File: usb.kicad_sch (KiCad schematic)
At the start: 3 parts, among them J4 USB_C_Receptacle_PowerOnly_6P

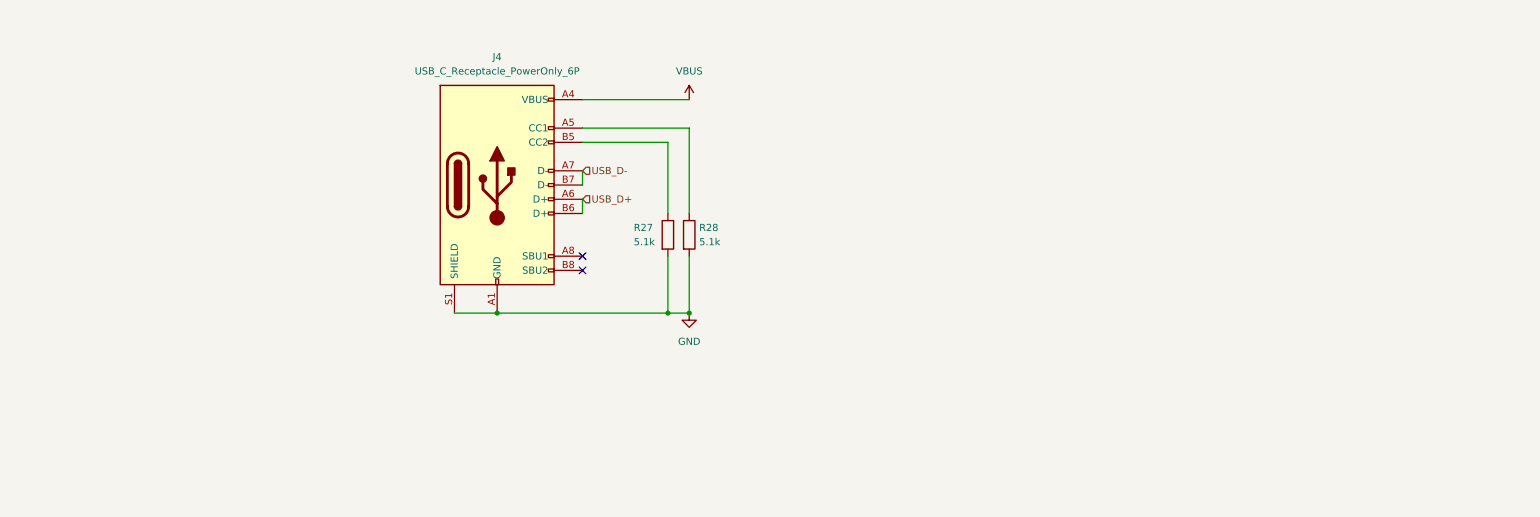
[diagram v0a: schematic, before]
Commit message: add audio amp
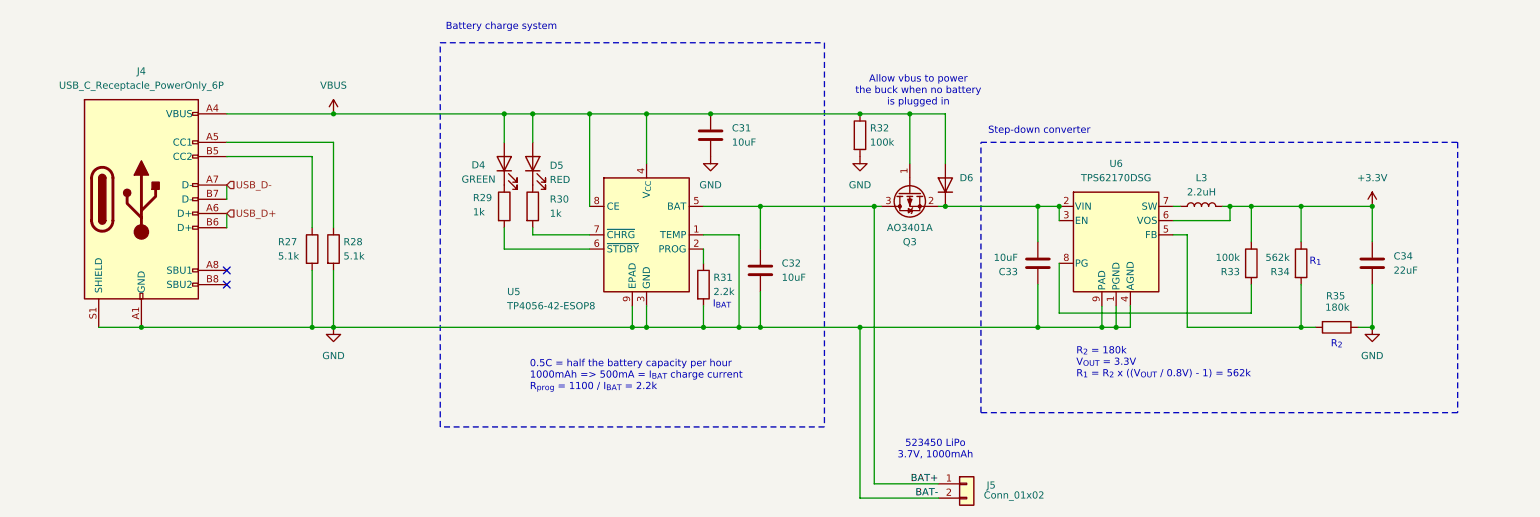
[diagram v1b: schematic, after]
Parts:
- added C31, C32, C33: 10uF, Capacitor_SMD:C_0603_1608Metric, symbol Device:C
- added C34: 22uF, Capacitor_SMD:C_0603_1608Metric, symbol Device:C
- added D4: GREEN, LED_SMD:LED_0603_1608Metric, symbol Device:LED
- added D5: RED, LED_SMD:LED_0603_1608Metric, symbol Device:LED
- added D6: D, Diode_SMD:D_SOD-323, symbol Device:D
- added J5: Conn_01x02, Connector_JST:JST_PH_B2B-PH-K_1x02_P2.00mm_Vertical, symbol Connector_Generic:Conn_01x02
- added L3: 2.2uH, Inductor_SMD:L_KOHERelec_MDA7030, symbol Device:L
- added Q3: AO3401A, Package_TO_SOT_SMD:SOT-23, symbol Transistor_FET:AO3401A
- added R29, R30: 1k, Resistor_SMD:R_0603_1608Metric, symbol Device:R
- added R31: 2.2k, Resistor_SMD:R_0603_1608Metric, symbol Device:R
- added R32, R33: 100k, Resistor_SMD:R_0603_1608Metric, symbol Device:R
- added R34: 562k, Resistor_SMD:R_0603_1608Metric, symbol Device:R
- added R35: 180k, Resistor_SMD:R_0603_1608Metric, symbol Device:R
- added U5: TP4056-42-ESOP8, Package_SO:SOIC-8-1EP_3.9x4.9mm_P1.27mm_EP2.41x3.3mm_ThermalVias, symbol Battery_Management:TP4056-42-ESOP8
- added U6: TPS62170DSG, Package_SON:WSON-8-1EP_2x2mm_P0.5mm_EP0.9x1.6mm_ThermalVias, symbol Regulator_Switching:TPS62170DSG
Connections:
- net GND: now also C31.2, C32.2, C33.2, C34.2, J5.2 (Pin_2), R31.2, R32.2, R35.1, U5.1 (TEMP), U5.3 (GND), U5.9 (EPAD), U6.1 (PGND), U6.4 (AGND), U6.9 (PAD)
- net VBUS: now also C31.1, D4.2 (A), D5.2 (A), D6.2 (A), Q3.1 (G), R32.1, U5.4 (V_{CC}), U5.8 (CE)
- new net: R33.2, U6.8 (PG)
- new net: D5.1 (K), R30.1
- new net: C33.1, D6.1 (K), Q3.2 (S), U6.2 (VIN), U6.3 (EN)
- new net: R31.1, U5.2 (PROG)
- new net: R29.2, U5.6 (~{STDBY})
- new net: R30.2, U5.7 (~{CHRG})
- new net: D4.1 (K), R29.1
- new net: R34.2, R35.2, U6.5 (FB)
- new net: L3.1, U6.7 (SW)
- new net +3.3V: C34.1, L3.2, R33.1, R34.1, U6.6 (VOS)
- new net BAT+: C32.1, J5.1 (Pin_1), Q3.3 (D), U5.5 (BAT)
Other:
- note added: "0.5C = half the battery capacity per hour 1000mAh => 500mA = I_{BAT} charge current R_{prog} = 1100 / I_{BAT} = 2.2k"
- note added: "523450 LiPo 3.7V, 1000mAh"
- note added: "Allow vbus to power the buck when no battery is plugged in"
- note added: "Battery charge system"
- note added: "I_{BAT}"
- note added: "R_{1}"
- note added: "R_{2}"
- note added: "R_{2} = 180k V_{OUT} = 3.3V R_{1} = R_{2} x ((V_{OUT} / 0.8V) - 1) = 562k"
- note added: "Step-down converter"
- moved on the sheet: J4, R27, R28

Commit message: add amplifier mode selector, add drawing lcd
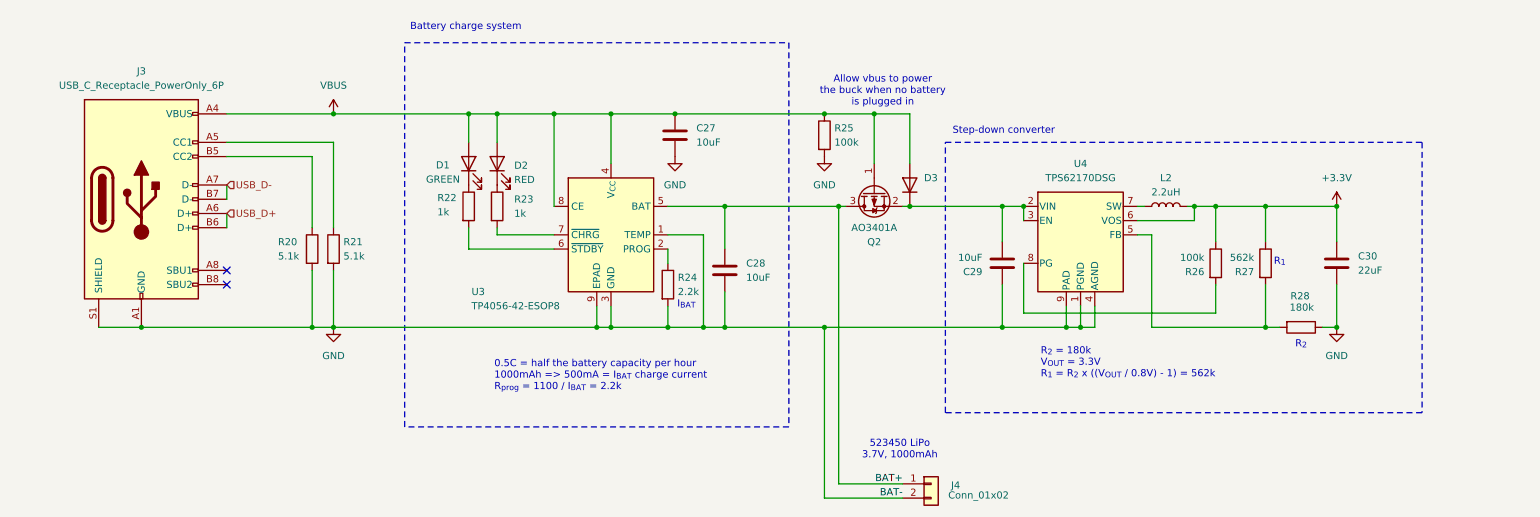
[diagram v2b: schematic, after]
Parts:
- renumbered C31 to C27, C32 to C28, C33 to C29, C34 to C30, D4 to D1, D5 to D2, D6 to D3, J4 to J3, J5 to J4, L3 to L2, Q3 to Q2, R27 to R20, R28 to R21, R29 to R22, R30 to R23, R31 to R24, R32 to R25, R33 to R26, R34 to R27, R35 to R28, U5 to U3, U6 to U4
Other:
- moved on the sheet: C27, C28, C29, C30, D1, D2, D3, J4, L2, Q2, R22, R23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

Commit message: add on/off switch
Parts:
- added SW12: SW_SPST, symbol Switch:SW_SPST
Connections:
- net +5V: now reaches C29.1, U4.2 (VIN), U4.3 (EN)
- net +5V: now also SW12.2 (B); no longer D3.1 (K), Q2.2 (S)
- new net: D3.1 (K), Q2.2 (S), SW12.1 (A)
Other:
- moved on the sheet: C27, C28, C29, C30, D1, D2, D3, J3, J4, L2, Q2, R20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

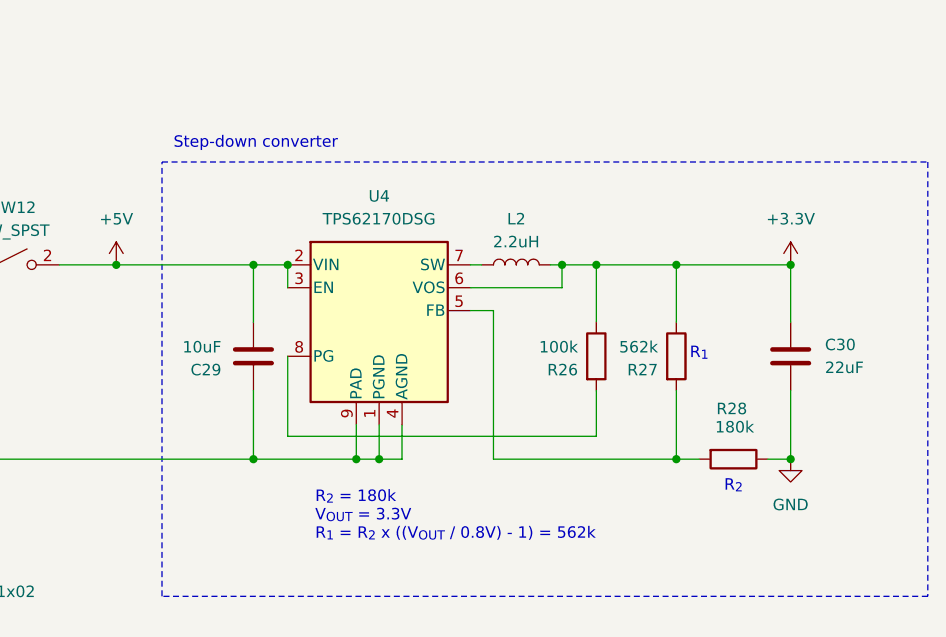
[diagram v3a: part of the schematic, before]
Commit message: add vibration motor
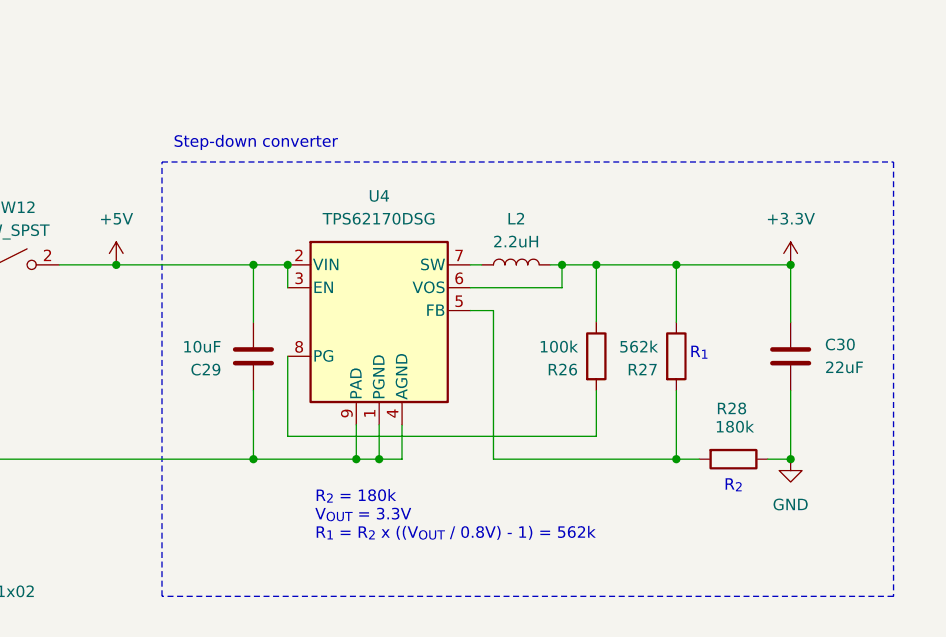
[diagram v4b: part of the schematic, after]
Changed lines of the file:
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@@
 	(rectangle
 		(start 198.12 73.66)
-		(end 283.21 121.92)
+		(end 279.4 121.92)
 		(stroke
 			(width 0)

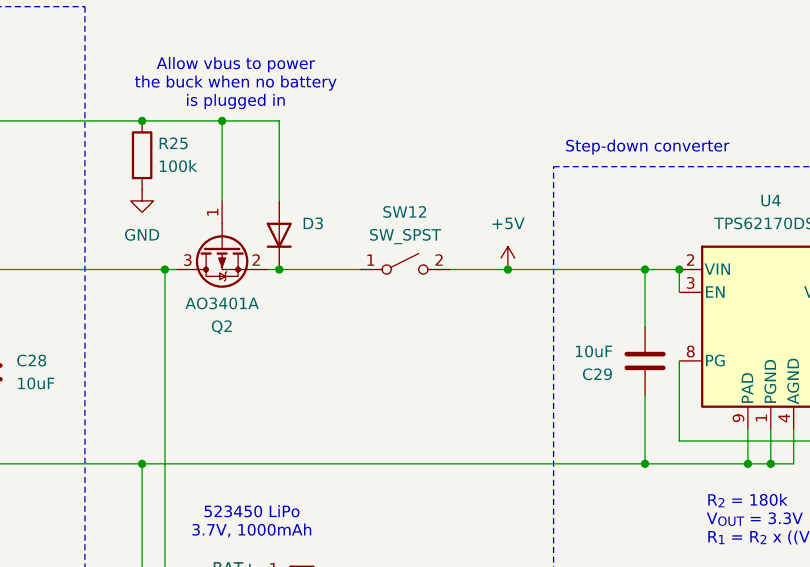
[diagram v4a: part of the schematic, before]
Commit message: add SD card
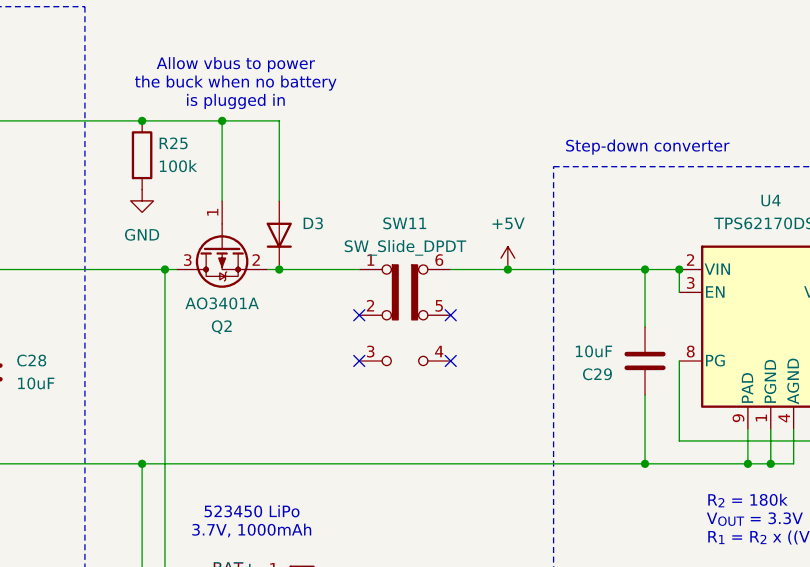
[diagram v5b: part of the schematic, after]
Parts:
- removed SW12: SW_SPST, symbol Switch:SW_SPST
- added SW11: SW_Slide_DPDT, Button_Switch_SMD:SW_DPDT_CK_JS202011JCQN, symbol Switch:SW_Slide_DPDT
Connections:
- net +5V: now also SW11.6 (C)
- net at D3.1 (K), Q2.2 (S): now also SW11.1 (A)
- no-connect marks 2 -> 6
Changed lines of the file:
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@@
+	)
+	(no_connect
+		(at 176.53 90.17)
+	)
+	(no_connect
+		(at 186.69 95.25)
+	)
+	(no_connect
+		(at 186.69 90.17)
 	)
 	(no_connect
 		(at 45.72 99.06)
+	)
+	(no_connect
+		(at 176.53 95.25)
 	)
 	(no_connect
@@
 	)
 	(symbol
-		(lib_id "Switch:SW_SPST")
-		(at 181.61 85.09 0)
+		(lib_id "Switch:SW_Slide_DPDT")
+		(at 181.61 90.17 0)
 		(unit 1)
 		(exclude_from_sim no)
@@
 		(dnp no)
 		(fields_autoplaced yes)
-		(property "Reference" "SW12"
-			(at 181.61 78.74 0)
-			(effects
-				(font
-					(size 1.27 1.27)
-				)
-			)
-		)
-		(property "Value" "SW_SPST"
-			(at 181.61 81.28 0)
-			(effects
-				(font
-					(size 1.27 1.27)
-				)
-			)
-		)
-		(property "Footprint" ""
-			(at 181.61 85.09 0)
+		(property "Reference" "SW11"
+			(at 181.61 80.01 0)
+			(effects
+				(font
+					(size 1.27 1.27)
+				)
+			)
+		)
+		(property "Value" "SW_Slide_DPDT"
+			(at 181.61 82.55 0)
+			(effects
+				(font
+					(size 1.27 1.27)
+				)
+			)
+		)
+		(property "Footprint" "Button_Switch_SMD:SW_DPDT_CK_JS202011JCQN"
+			(at 195.58 85.09 0)
 			(effects
 				(font
@@
 		)
 		(property "Datasheet" "~"
-			(at 181.61 85.09 0)
-			(effects
-				(font
-					(size 1.27 1.27)
-				)
-				(hide yes)
-			)
-		)
-		(property "Description" "Single Pole Single Throw (SPST) switch"
-			(at 181.61 85.09 0)
-			(effects
-				(font
-					(size 1.27 1.27)
-				)
-				(hide yes)
-			)
+			(at 181.61 90.17 0)
+			(effects
+				(font
+					(size 1.27 1.27)
+				)
+				(hide yes)
+			)
+		)
+		(property "Description" "Slide Switch, dual pole double throw"
+			(at 181.61 90.17 0)
+			(effects
+				(font
+					(size 1.27 1.27)
+				)
+				(hide yes)
+			)
+		)
+		(property "LCSC" "C221665"
+			(at 181.61 90.17 0)
+			(effects
+				(font
+					(size 1.27 1.27)
+				)
+				(hide yes)
+			)
+		)
+		(property "Manufacturer" "C&K"
+			(at 181.61 90.17 0)
+			(effects
+				(font
+					(size 1.27 1.27)
+				)
+				(hide yes)
+			)
+		)
+		(property "Manufacturer Part Number" "JS202011JCQN"
+			(at 181.61 90.17 0)
+			(effects
+				(font
+					(size 1.27 1.27)
+				)
+				(hide yes)
+			)
+		)
+		(pin "3"
+		)
+		(pin "6"
+		)
+		(pin "4"
+		)
+		(pin "1"
 		)
 		(pin "2"
 		)
-		(pin "1"
+		(pin "5"
 		)
 		(instances
 			(project ""
 				(path "/f4643692-c319-40a7-82a2-3e775c0a417f/14ac419d-87de-4e8e-be3d-9259b1e7c76f"
-					(reference "SW12")
+					(reference "SW11")
 					(unit 1)
 				)

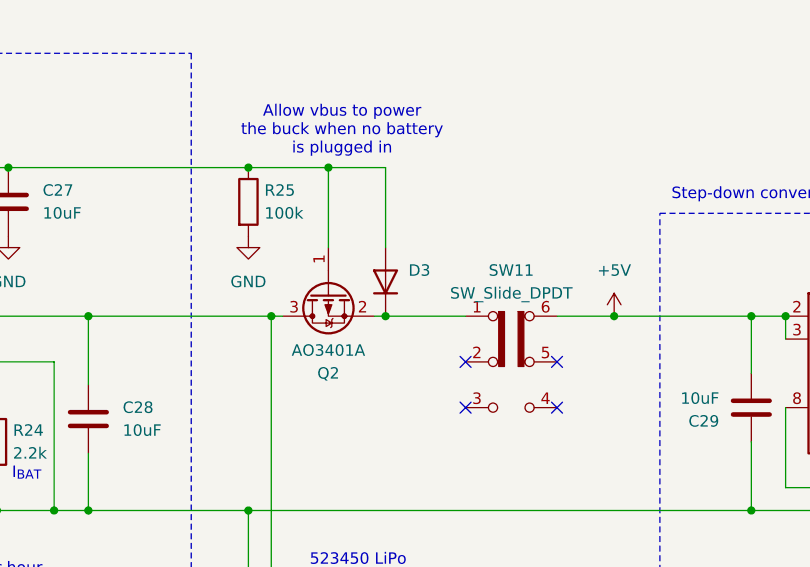
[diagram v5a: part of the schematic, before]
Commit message: small updates in component selection
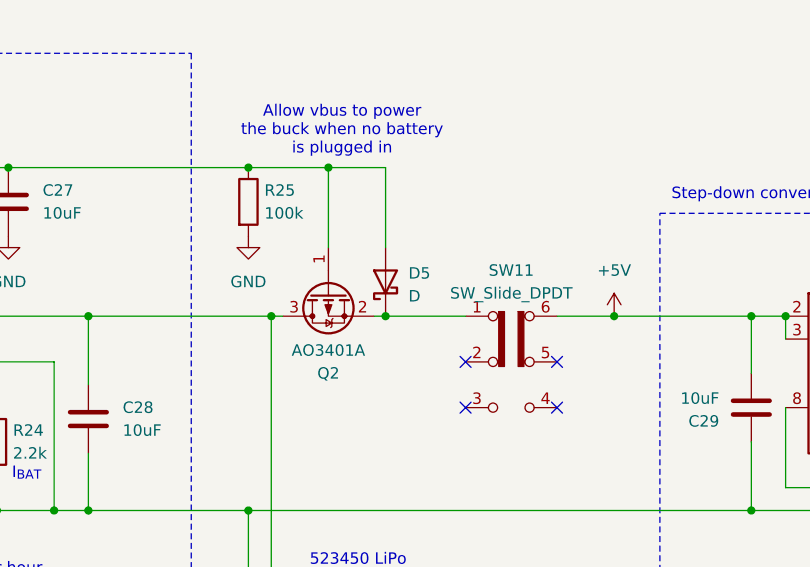
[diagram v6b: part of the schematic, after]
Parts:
- removed D3: D, Diode_SMD:D_SOD-323, symbol Device:D
- added D5: D, Diode_SMD:D_SMA, symbol Device:D_Schottky
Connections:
- net VBUS: now also D5.2 (A)
- net at Q2.2 (S), SW11.1 (A): now also D5.1 (K)
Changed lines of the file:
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@@
 	)
 	(junction
-		(at 114.3 106.68)
+		(at 167.64 85.09)
 		(diameter 0)
 		(color 0 0 0 0)
 	)
 	(junction
-		(at 167.64 85.09)
+		(at 114.3 106.68)
 		(diameter 0)
 		(color 0 0 0 0)
@@
 	(wire
 		(pts
+			(xy 167.64 85.09) (xy 176.53 85.09)
+		)
+		(stroke
+			(width 0)
+			(type default)
+		)
+	)
+	(wire
+		(pts
 			(xy 186.69 85.09) (xy 193.04 85.09)
 		)
@@
 	(wire
 		(pts
-			(xy 167.64 85.09) (xy 176.53 85.09)
-		)
-		(stroke
-			(width 0)
-			(type default)
-		)
-	)
-	(wire
-		(pts
 			(xy 111.76 102.87) (xy 111.76 106.68)
 		)
@@
 	)
 	(symbol
+		(lib_id "Device:D_Schottky")
+		(at 167.64 81.28 90)
+		(unit 1)
+		(exclude_from_sim no)
+		(in_bom yes)
+		(on_board yes)
+		(dnp no)
+		(fields_autoplaced yes)
+		(property "Reference" "D5"
+			(at 170.18 80.3274 90)
+			(effects
+				(font
+					(size 1.27 1.27)
+				)
+				(justify right)
+			)
+		)
+		(property "Value" "D"
+			(at 170.18 82.8674 90)
+			(effects
+				(font
+					(size 1.27 1.27)
+				)
+				(justify right)
+			)
+		)
+		(property "Footprint" "Diode_SMD:D_SMA"
+			(at 167.64 81.28 0)
+			(effects
+				(font
+					(size 1.27 1.27)
+				)
+				(hide yes)
+			)
+		)
+		(property "Datasheet" "~"
+			(at 167.64 81.28 0)
+			(effects
+				(font
+					(size 1.27 1.27)
+				)
+				(hide yes)
+			)
+		)
+		(property "Description" "Schottky diode"
+			(at 167.64 81.28 0)
+			(effects
+				(font
+					(size 1.27 1.27)
+				)
+				(hide yes)
+			)
+		)
+		(property "Sim.Device" "D"
+			(at 167.64 81.28 0)
+			(effects
+				(font
+					(size 1.27 1.27)
+				)
+				(hide yes)
+			)
+		)
+		(property "Sim.Pins" "1=K 2=A"
+			(at 167.64 81.28 0)
+			(effects
+				(font
+					(size 1.27 1.27)
+				)
+				(hide yes)
+			)
+		)
+		(property "LCSC" "C64982"
+			(at 167.64 81.28 0)
+			(effects
+				(font
+					(size 1.27 1.27)
+				)
+				(hide yes)
+			)
+		)
+		(property "Manufacturer" "MDD(Microdiode Semiconductor)"
+			(at 167.64 81.28 0)
+			(effects
+				(font
+					(size 1.27 1.27)
+				)
+				(hide yes)
+			)
+		)
+		(property "Manufacturer Part Number" "B340A"
+			(at 167.64 81.28 0)
+			(effects
+				(font
+					(size 1.27 1.27)
+				)
+				(hide yes)
+			)
+		)
+		(pin "1"
+		)
+		(pin "2"
+		)
+		(instances
+			(project "gameboy"
+				(path "/f4643692-c319-40a7-82a2-3e775c0a417f/14ac419d-87de-4e8e-be3d-9259b1e7c76f"
+					(reference "D5")
+					(unit 1)
+				)
+			)
+		)
+	)
+	(symbol
 		(lib_id "Device:R")
 		(at 246.38 95.25 0)
@@
 					(unit 1)
 				)
-			)
-		)
-	)
-	(symbol
-		(lib_id "Device:D")
-		(at 167.64 81.28 90)
-		(unit 1)
-		(exclude_from_sim no)
-		(in_bom yes)
-		(on_board yes)
-		(dnp no)
-		(fields_autoplaced yes)
-		(property "Reference" "D3"
-			(at 170.18 80.0099 90)
-			(effects
-				(font
-					(size 1.27 1.27)
-				)
-				(justify right)
-			)
-		)
-		(property "Value" "D"
-			(at 170.18 82.5499 90)
-			(effects
-				(font
-					(size 1.27 1.27)
-				)
-				(justify right)
-				(hide yes)
-			)
-		)
-		(property "Footprint" "Diode_SMD:D_SOD-323"
-			(at 167.64 81.28 0)
-			(effects
-				(font
-					(size 1.27 1.27)
-				)
-				(hide yes)
-			)
-		)
-		(property "Datasheet" "~"
-			(at 167.64 81.28 0)
-			(effects
-				(font
-					(size 1.27 1.27)
-				)
-				(hide yes)
-			)
-		)
-		(property "Description" "Diode"
-			(at 167.64 81.28 0)
-			(effects
-				(font
-					(size 1.27 1.27)
-				)
-				(hide yes)
-			)
-		)
-		(property "Sim.Device" "D"
-			(at 167.64 81.28 0)
-			(effects
-				(font
-					(size 1.27 1.27)
-				)
-				(hide yes)
-			)
-		)
-		(property "Sim.Pins" "1=K 2=A"
-			(at 167.64 81.28 0)
-			(effects
-				(font
-					(size 1.27 1.27)
-				)
-				(hide yes)
-			)
-		)
-		(property "LCSC" "C191023"
-			(at 167.64 81.28 0)
-			(effects
-				(font
-					(size 1.27 1.27)
-				)
-				(hide yes)
-			)
-		)
-		(property "Manufacturer" "Guangdong Hottech"
-			(at 167.64 81.28 0)
-			(effects
-				(font
-					(size 1.27 1.27)
-				)
-				(hide yes)
-			)
-		)
-		(property "Manufacturer Part Number" "1N5819WS"
-			(at 167.64 81.28 0)
-			(effects
-				(font
-					(size 1.27 1.27)
-				)
-				(hide yes)
-			)
-		)
-		(pin "2"
-		)
-		(pin "1"
-		)
-		(instances
-			(project "gameboy"
-				(path "/f4643692-c319-40a7-82a2-3e775c0a417f/14ac419d-87de-4e8e-be3d-9259b1e7c76f"
-					(reference "D3")
-					(unit 1)
-				)
